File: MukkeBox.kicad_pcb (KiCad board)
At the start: 2 copper layers, 200 x 105 mm, 303 parts, among them J101 ST_Link_V2_10P, J104 Conn_02x05_Odd_Even, J107 PinHeader, J108 PinHeader, J109 PinHeader, J201 TB001-500-07BE CUI_Devices, J301 Conn_02x04_Odd_Even, J302 Conn_02x04_Odd_Even, J401 TB001-500-02BE CUI_Devices, J501 TB001-500-04BE CUI_Devices, J601 Conn_01x03_Female, J602 Conn_02x01, J801 Conn_01x05, J802 Conn_01x04, Q101 NTK3043N, Q201 NTD14N03RT4G, Q202 NTD14N03RT4G, Q203 NTD14N03RT4G, Q301 MMBT2222LT1G, Q302 TK7R7P10PL, Q401 NTK3043N, Q402 FDD4685-F085, SW501 DS04-254-2-02BK-SMT, U101 TPS7B82-Q1, U102 STM32F030C6Tx_MukkeBox, U201 BQ76920, U202 BQ76200, U301 L7812, U302 UC3843_SOIC8, U401 MAX1873TEEE, U402 PC827, U501 TDA7498L, U601 XC6216C, U602 TDA7418, U701 XS3868, U801 MCP23017_SO, Y101 FOXSDLF/080-20

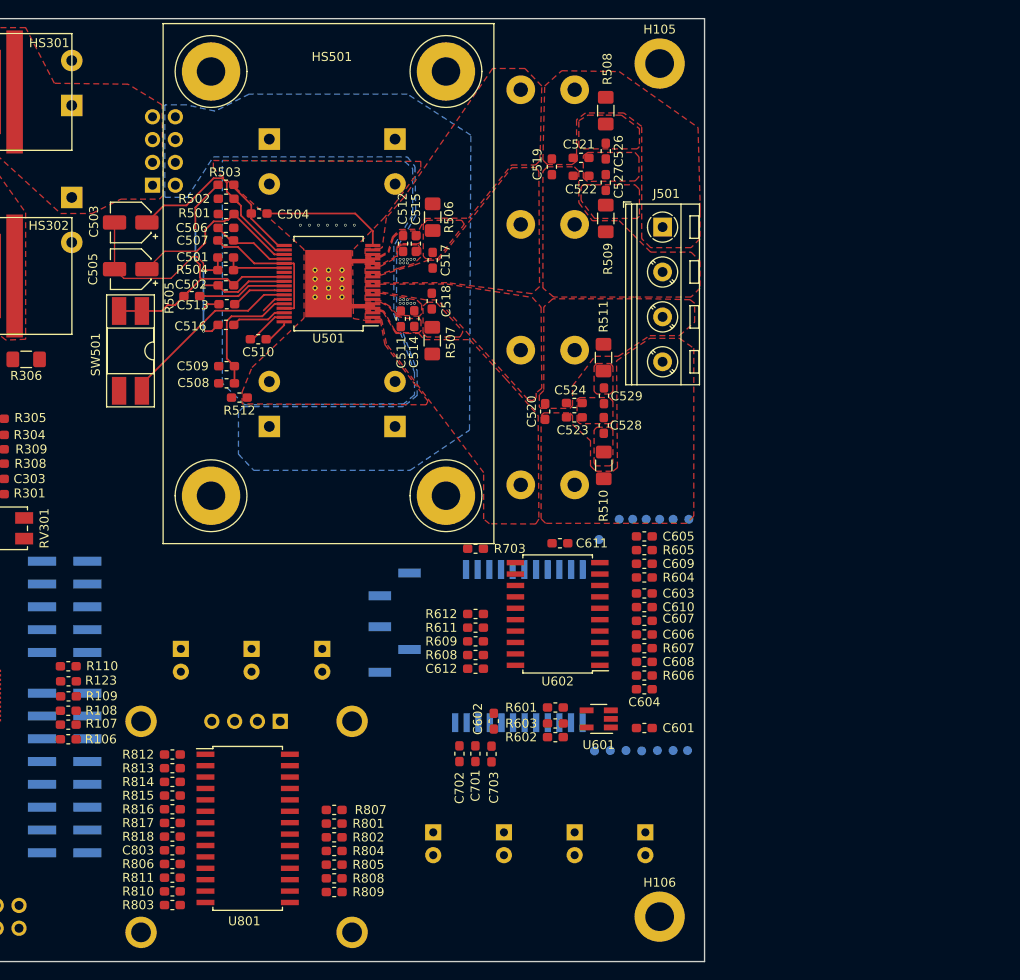
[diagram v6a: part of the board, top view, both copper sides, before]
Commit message: Folienkondensatoren SMD gegen THT ausgetauscht. Kleine Fehler korrigiert
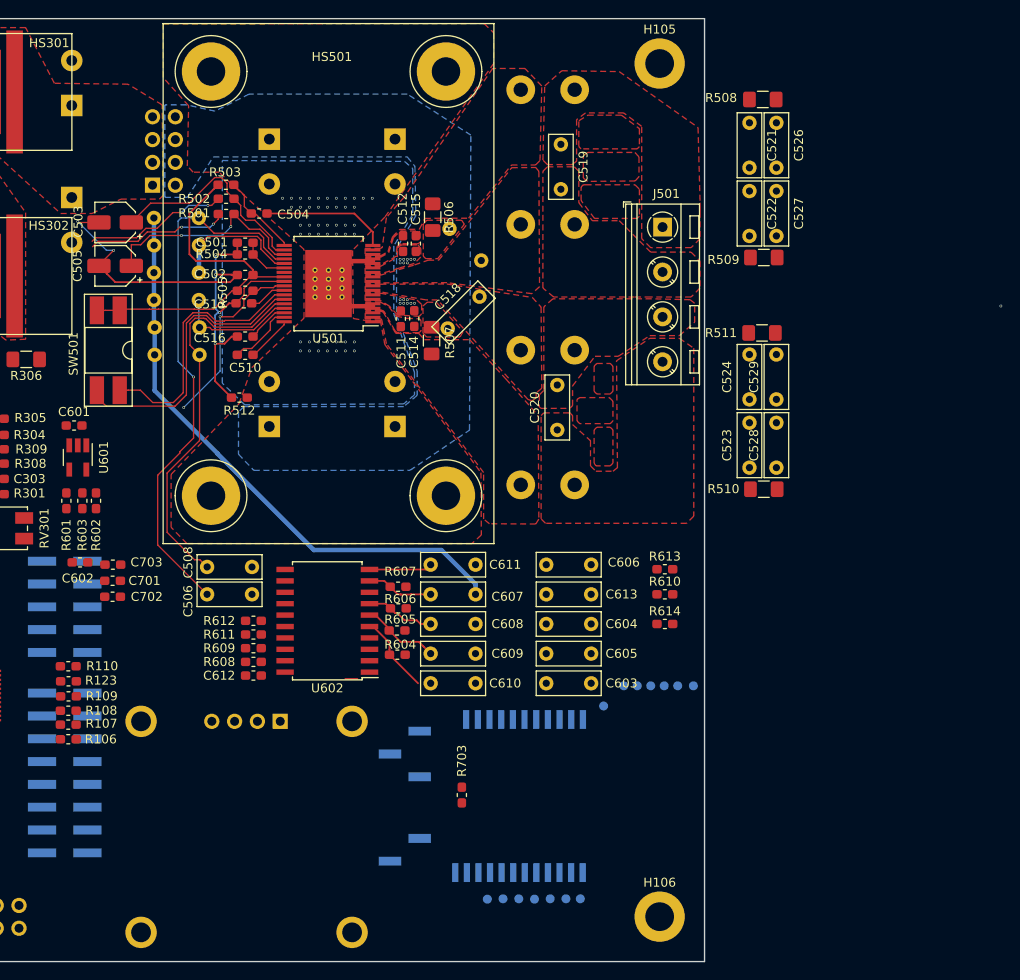
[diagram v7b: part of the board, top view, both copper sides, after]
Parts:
- removed C803: 100nF, Capacitor_SMD:C_0603_1608Metric_Pad1.05x0.95mm_HandSolder
- removed D801: LED_25%, LED_THT:LED_D5.0mm
- removed D802: LED_50%, LED_THT:LED_D5.0mm
- removed D803: LED_75%, LED_THT:LED_D5.0mm
- removed D804: LED_100%, LED_THT:LED_D5.0mm
- removed D805: LED_FAULT, LED_THT:LED_D5.0mm
- removed D806, D807: AUX, LED_THT:LED_D5.0mm
- removed R801, R804, R808: DNP, Resistor_SMD:R_0603_1608Metric_Pad1.05x0.95mm_HandSolder
- removed R802, R805, R809: 0R, Resistor_SMD:R_0603_1608Metric_Pad1.05x0.95mm_HandSolder
- removed R803, R806: 3K3, Resistor_SMD:R_0603_1608Metric_Pad1.05x0.95mm_HandSolder
- removed R807: 10K, Resistor_SMD:R_0603_1608Metric_Pad1.05x0.95mm_HandSolder
- removed R810, R811: 47R, Resistor_SMD:R_0603_1608Metric_Pad1.05x0.95mm_HandSolder
- removed R812, R813, R814, R815, R816, R817, R818: 1K, Resistor_SMD:R_0603_1608Metric_Pad1.05x0.95mm_HandSolder
- removed U801: MCP23017_SO, Package_SO:SOIC-28W_7.5x17.9mm_P1.27mm
- added C533: 1uF, Capacitor_THT:C_Rect_L7.0mm_W2.5mm_P5.00mm, B.Cu at (184.2, 68.4)
- added C534: 1nF, Capacitor_THT:C_Rect_L7.0mm_W2.5mm_P5.00mm, B.Cu at (189.2, 74.5)
- added C535: 1uF, Capacitor_THT:C_Rect_L7.0mm_W2.5mm_P5.00mm, B.Cu at (184.2, 65.4)
- added C536: 1nF, Capacitor_THT:C_Rect_L7.0mm_W2.5mm_P5.00mm, B.Cu at (189.2, 62.3)
- added C613: 1uF, Capacitor_THT:C_Rect_L7.0mm_W2.5mm_P5.00mm, F.Cu at (227.8, 101.2)
- added R610: 47K, Resistor_SMD:R_0603_1608Metric_Pad1.05x0.95mm_HandSolder, F.Cu at (241.0, 101.2)
- added R613: 47K, Resistor_SMD:R_0603_1608Metric_Pad1.05x0.95mm_HandSolder, F.Cu at (241.0, 98.4)
- added R614: 47K, Resistor_SMD:R_0603_1608Metric_Pad1.05x0.95mm_HandSolder, F.Cu at (241.0, 104.5)
- C506, C508, C518, C519, C520, C521, C522, C523, C524, C526, C527, C528, C529, C603, C604, C605, C606, C607, C608, C609, C610: footprint Capacitor_SMD:C_0603_1608Metric_Pad1.05x0.95mm_HandSolder -> Capacitor_THT:C_Rect_L7.0mm_W2.5mm_P5.00mm
- C507, C509, C517: footprint Capacitor_SMD:C_0603_1608Metric_Pad1.05x0.95mm_HandSolder -> Capacitor_THT:C_Rect_L7.0mm_W2.5mm_P5.00mm; moved to B.Cu
- C611: value 100nF -> 100nF 5%; footprint Capacitor_SMD:C_0603_1608Metric_Pad1.05x0.95mm_HandSolder -> Capacitor_THT:C_Rect_L7.0mm_W2.5mm_P5.00mm
- moved C601 71.9 mm to (175.3, 82.4), turned to 0 degrees
- moved U601 64.9 mm to (175.7, 86.0), turned to 270 degrees
- moved R601 59.1 mm to (174.4, 90.8), turned to 270 degrees
- moved R603 58.2 mm to (176.2, 90.8), turned to 270 degrees
- moved R602 57.5 mm to (177.7, 90.8), turned to 270 degrees
- moved C602 49.3 mm to (175.9, 97.6), turned to 0 degrees
- moved C703 47.1 mm to (179.6, 97.9), turned to 180 degrees
- moved C701 44.8 mm to (179.5, 99.7), turned to 0 degrees
- moved C702 42.4 mm to (179.5, 101.5), turned to 0 degrees
- moved C506 40.9 mm to (195.1, 101.2)
- moved J602 29.6 mm to (212.1, 129.6)
- moved R605 29.0 mm to (211.2, 105.2), turned to 0 degrees
- moved R604 28.8 mm to (211.3, 107.9), turned to 0 degrees
- moved R606 28.4 mm to (211.4, 102.8)
- moved R607 28.3 mm to (211.3, 100.3), turned to 0 degrees
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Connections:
- net /AudioProcessor/AUX_L renamed Net-(C604-Pad2)
- C110 pad 1: Net-(C110-Pad1) -> GND
- C110 pad 2: GND -> /BASS
- C111 pad 1: Net-(C111-Pad1) -> GND
- C111 pad 2: GND -> /GAIN
- C112 pad 1: GND -> /TREBLE
- C112 pad 2: Net-(C112-Pad2) -> GND
- C113 pad 1: GND -> /MIDDLE
- C113 pad 2: Net-(C113-Pad2) -> GND
- C507 pad 1: Net-(C506-Pad2) -> GNDA
- C507 pad 2: GNDA -> Net-(C506-Pad2)
- C509 pad 1: Net-(C508-Pad2) -> Net-(C509-Pad1)
- J108 pad 11: Net-(C112-Pad2) -> Net-(J108-Pad11)
- J108 pad 2: Net-(C111-Pad1) -> Net-(J108-Pad2)
- J108 pad 5: Net-(C110-Pad1) -> Net-(J108-Pad5)
- J108 pad 8: Net-(C113-Pad2) -> Net-(J108-Pad8)
- J601 pad 1: GNDA -> Net-(C613-Pad2)
- R119 pad 1: Net-(C111-Pad1) -> Net-(J108-Pad2)
- R120 pad 1: Net-(C110-Pad1) -> Net-(J108-Pad5)
- R121 pad 1: Net-(C113-Pad2) -> Net-(J108-Pad8)
- R122 pad 1: Net-(C112-Pad2) -> Net-(J108-Pad11)
- U501 pad 23: GNDA -> Net-(C535-Pad2)
- U501 pad 33: GNDA -> Net-(C509-Pad1)
- U602 pad 3: Net-(C608-Pad2) -> Net-(U602-Pad3)
- U602 pad 4: Net-(C607-Pad2) -> Net-(U602-Pad4)
- U602 pad 7: Net-(U602-Pad7) -> Net-(C608-Pad2)
- U602 pad 9: Net-(U602-Pad9) -> Net-(C607-Pad2)
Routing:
- net Net-(C506-Pad2): track 8.80 -> 60.7 mm, vias 0 -> 1
- net GNDA: track 15.6 -> 65.1 mm
- net Net-(SW501-Pad3): track 2.81 -> 32.4 mm
- net Net-(C508-Pad2): track 14.5 -> 43.5 mm
- net GNDS: track 41.3 -> 61.9 mm, vias 4 -> 6
- net STBY_TDA7498: track 0.00 -> 16.0 mm, vias 0 -> 2
- net MUTE_TDA7498: track 0.00 -> 15.8 mm, vias 0 -> 2
- net Net-(C535-Pad2): track 0.00 -> 14.8 mm
- net Net-(C509-Pad1): track 0.00 -> 13.6 mm
- net DIAG_TDA7498: track 9.89 -> 20.7 mm, vias 0 -> 2
- net Net-(C610-Pad2): track 0.00 -> 10.2 mm
- net Net-(C609-Pad2): track 0.00 -> 8.70 mm
- net Net-(SW501-Pad4): track 20.7 -> 29.2 mm
- net /Amplifier/VDDS: track 32.4 -> 40.2 mm, vias 2 -> 0
- net Net-(C608-Pad2): track 0.00 -> 7.74 mm
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
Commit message: layout fast fertig
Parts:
- removed C506, C508: 1uF, Capacitor_THT:C_Rect_L7.0mm_W2.5mm_P5.00mm
- removed TP701: CH_POWER, TestPoint:TestPoint_Pad_D1.0mm
- removed TP702: CHARGE, TestPoint:TestPoint_Pad_D1.0mm
- removed TP703: STAT, TestPoint:TestPoint_Pad_D1.0mm
- removed TP704: TP MIC-, TestPoint:TestPoint_Pad_D1.0mm
- removed TP705: TP MIC+, TestPoint:TestPoint_Pad_D1.0mm
- removed TP706: GNDA_TP, TestPoint:TestPoint_Pad_D1.0mm
- removed TP707: Play, TestPoint:TestPoint_Pad_D1.0mm
- removed TP708: Back, TestPoint:TestPoint_Pad_D1.0mm
- removed TP709: Next, TestPoint:TestPoint_Pad_D1.0mm
- removed TP710: ---, TestPoint:TestPoint_Pad_D1.0mm
- removed TP711: 42, TestPoint:TestPoint_Pad_D1.0mm
- removed TP712: Vol-, TestPoint:TestPoint_Pad_D1.0mm
- removed TP713: Vol+, TestPoint:TestPoint_Pad_D1.0mm
- removed TP714: TestPoint, TestPoint:TestPoint_Pad_D1.0mm
- added C614: 1uF, Capacitor_THT:C_Rect_L7.0mm_W2.5mm_P5.00mm, B.Cu at (182.9, 110.6)
- added C615: 1uF, Capacitor_THT:C_Rect_L7.0mm_W2.5mm_P5.00mm, B.Cu at (182.9, 107.5)
- added C616: 1uF, Capacitor_THT:C_Rect_L7.0mm_W2.5mm_P5.00mm, B.Cu at (182.9, 104.4)
- added J603: Conn_02x05_Odd_Even, Connector_PinHeader_2.54mm:PinHeader_2x05_P2.54mm_Vertical_SMD, B.Cu at (203.6, 104.2)
- added R615: 1K, Resistor_SMD:R_0603_1608Metric_Pad1.05x0.95mm_HandSolder, F.Cu at (194.8, 98.4)
- added R616: 1K, Resistor_SMD:R_0603_1608Metric_Pad1.05x0.95mm_HandSolder, F.Cu at (194.8, 96.6)
- added R617: 100K, Resistor_SMD:R_0603_1608Metric_Pad1.05x0.95mm_HandSolder, F.Cu at (211.3, 111.9)
- added R618: 1K, Resistor_SMD:R_0603_1608Metric_Pad1.05x0.95mm_HandSolder, F.Cu at (211.3, 110.1)
- added R619: 1K, Resistor_SMD:R_0603_1608Metric_Pad1.05x0.95mm_HandSolder, F.Cu at (211.3, 98.6)
- added R620: 1K, Resistor_SMD:R_0603_1608Metric_Pad1.05x0.95mm_HandSolder, F.Cu at (211.4, 97.1)
- C518, C603, C604, C605, C606, C607, C608, C609, C610, C611, C613: moved to B.Cu
- C801, C802, U701: moved to F.Cu
- moved J802 95.3 mm to (219.9, 138.1)
- moved C801 95.1 mm to (197.0, 118.7), turned to 180 degrees
- moved C802 82.2 mm to (213.5, 137.7)
- moved J602 52.9 mm to (181.2, 86.7), turned to 0 degrees
- moved J601 30.1 mm to (240.9, 110.3)
- moved R510 22.5 mm to (230.0, 93.9)
- moved R511 18.1 mm to (233.9, 70.3)
- moved R509 17.6 mm to (234.5, 63.7), turned to 270 degrees
- moved R508 17.0 mm to (235.5, 41.7), turned to 270 degrees
- moved C529 17.0 mm to (237.6, 85.5)
- moved C523 17.0 mm to (234.6, 93.0)
- moved C528 17.0 mm to (237.6, 93.0)
- moved U701 16.7 mm to (216.4, 115.5), turned to 270 degrees
- moved C527 16.3 mm to (237.3, 54.9), turned to 0 degrees
- moved C524 16.1 mm to (234.4, 78.5)
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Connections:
- net Net-(C604-Pad2) renamed /AudioProcessor/AUX_L
- C507 pad 2: Net-(C506-Pad2) -> TO_SPEAKER_L
- C534 pad 1: Net-(C508-Pad2) -> TO_SPEAKER_R
- C606 pad 2: /AudioProcessor/AUX_R -> Net-(C606-Pad2)
- C611 pad 1: GND -> GNDA
- C613 pad 2: Net-(C613-Pad2) -> /AudioProcessor/AUX_R
- J601 pad 1: Net-(C613-Pad2) -> Net-(C606-Pad2)
- R610 pad 2: Net-(C613-Pad2) -> Net-(C606-Pad2)
- U501 pad 22: Net-(C506-Pad2) -> TO_SPEAKER_L
- U501 pad 32: Net-(C508-Pad2) -> TO_SPEAKER_R
- U602 pad 13: TO_SPEAKER_R -> Net-(C615-Pad1)
- U602 pad 16: TO_SPEAKER_L -> Net-(C614-Pad1)
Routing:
- net +3V3: track 0.00 -> 364.9 mm, vias 0 -> 9
- net CHARGER_DISABLE: track 0.00 -> 250.3 mm, vias 0 -> 2
- net CHARGER_IOUT: track 2.41 -> 200.7 mm
- net CHARGER_PLUGGED: track 7.85 -> 197.6 mm, vias 0 -> 4
- net CP_EN: track 0.00 -> 176.6 mm, vias 0 -> 4
- net SYSTEM_LOAD: track 0.00 -> 175.0 mm, vias 0 -> 2
- net SDA: track 0.00 -> 161.5 mm, vias 0 -> 3
- net SCL: track 0.00 -> 153.8 mm, vias 0 -> 3
- net PMON_EN: track 0.00 -> 146.4 mm, vias 0 -> 2
- net PCHG_EN: track 0.00 -> 144.6 mm, vias 0 -> 2
- net CELL1_SENSE: track 11.3 -> 149.9 mm, vias 0 -> 3
- net BATTERY+: track 0.00 -> 133.5 mm, vias 0 -> 18
- net PACK_VOLTAGE: track 0.00 -> 129.0 mm, vias 0 -> 2
- net ALERT_BQ76920: track 0.00 -> 127.7 mm, vias 0 -> 4
- net GND: track 11.8 -> 135.2 mm, vias 0 -> 52
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- added copper zone on F.Cu, net /00_Charger/DC_20V_POWER_SUPPLY
- added copper zone on F.Cu, net /00_Charger/POWER_SUPPLY
- added copper zone on B.Cu, net /01_BMS/CELL4_SENSE
- added copper zone on B.Cu, net BATTERY+
- added copper zone on F.Cu, net BATTERY+
- added copper zone on B.Cu, net GND
- added copper zone on F.Cu, net GND
- added copper zone on F.Cu, net Net-(HS201-Pad1)
- added copper zone on F.Cu, net Net-(L401-Pad2)
- added copper zone on F.Cu, net Net-(Q202-Pad3)
- added copper zone on B.Cu, net Net-(Q302-Pad3)
- added copper zone on F.Cu, net Net-(Q302-Pad3)
- added copper zone on B.Cu, net PACK+
- added copper zone on F.Cu, net PACK+
- removed copper zone on F.Cu, net Net-(C527-Pad2)
- removed copper zone on F.Cu, net Net-(C528-Pad1)
- removed copper zone on F.Cu, net Net-(C529-Pad2)
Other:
- rule trace_min: 0.1 -> 0.15
